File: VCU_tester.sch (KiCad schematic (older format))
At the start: 49 parts, among them J1 Conn_01x04_Male, J12 Conn_01x08_Male, J13 Conn_01x08_Male, J14 USB_C_Receptacle, J15 USB_B_Micro, J2 Screw_Terminal_01x02, J500 Conn_01x10_Female, J501 Conn_01x08_Female, J502 Conn_01x08_Female, J503 Conn_01x08_Female, J504 Conn_01x08_Female, J505 Conn_01x08_Female, J507 Conn_02x18_Odd_Even, J7 Conn_01x04_Male, P8 BeagleBone_Black_Header, P9 BeagleBone_Black_Header, U1 REF3020, U6 DS3231MZ, U7 DS3231MZ

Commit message: better routing, tcan footprint, mount holes + silkscreen
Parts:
- added H1, H2, H3, H4, H5, H6: MountingHole, MountingHole:MountingHole_3.2mm_M3_ISO7380_Pad, symbol Mechanical:MountingHole
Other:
- note added: "Removed (TO REASSIGN):\n J507-4 (adc) to GPIO_45\n J507-5 (adc) to GPIO_46\n J507-9 (uart) to GPIO_50\n J507-10 (nc) to GPIO_51"
- note added: "TODO:\n0) Assign new GPIOs on VCU\n1) ADD SILKSCREEN FOR WHAT TESTPOINTS ARE!!! (GPIO out of VCU??)"
- note removed: "Changes made (Andrew):\nPD25 (J500-3) fixed to VCURXD2A\nPressLin,PressLout moved to correct pins\nJ507-10 corrected to NC\nConnection to RTC Beagle fixed: SCL/SDA swapped\nRemoved:\n J507-4 (adc) to GPIO_45\n J507-5 (adc) to GPIO_46\n J507-9 (uart) to GPIO_50\n J507-10 (nc) to GPIO_51"
- note removed: "Changes made (Will):\nBoard initial layout done (NEED GPIOs)\nChanged power bus\n"
- note removed: "TODO:\n0) Assign new GPIOs on VCU\n1) ADD RES TO CP1/2 ON USBC\n2) ADD SILKSCREEN FOR WHAT TESTPOINTS ARE!!! (GPIO out of VCU??)"
- note removed: "\nReview gpio assignments\n"
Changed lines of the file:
@@
 Wire Wire Line
 	2800 7450 3700 7450
-Text Notes -2600 -2800 0    100  ~ 0
-Changes made (Andrew):\nPD25 (J500-3) fixed to VCURXD2A\nPressLin,PressLout moved to correct pins\nJ507-10 corrected to NC\nConnection to RTC Beagle fixed: SCL/SDA swapped\nRemoved:\n  J507-4 (adc) to GPIO_45\n  J507-5 (adc) to GPIO_46\n  J507-9 (uart) to GPIO_50\n  J507-10 (nc) to GPIO_51
+Text Notes -2600 -600 0    100  ~ 0
+Removed (TO REASSIGN):\n  J507-4 (adc) to GPIO_45\n  J507-5 (adc) to GPIO_46\n  J507-9 (uart) to GPIO_50\n  J507-10 (nc) to GPIO_51
 NoConn ~ 5300 7350
 NoConn ~ 5300 7450
@@
 NoConn ~ 5800 7550
 NoConn ~ 5800 7450
-Text Notes -2600 -950 0    100  ~ 0
-\nReview gpio assignments\n
 NoConn ~ 5300 8550
 Text Notes 5850 8550 0    50   ~ 0
@@
 	0    -1   -1   0
 $EndComp
-Text Notes 5450 -400 0    197  Italic 39
+Text Notes -4950 -2450 0    197  Italic 39
 wtf is up with VCU{TX,RX}D2 and VCU{TX,RX}D2A ???
 $Comp
@@
 $EndComp
 Text Notes -2600 -1750 0    79   ~ 16
-TODO:\n0) Assign new GPIOs on VCU\n1) ADD RES TO CP1/2 ON USBC\n2) ADD SILKSCREEN FOR WHAT TESTPOINTS ARE!!! (GPIO out of VCU??)
-Text Notes 2100 -1900 0    100  ~ 0
-Changes made (Will):\nBoard initial layout done (NEED GPIOs)\nChanged power bus\n
+TODO:\n0) Assign new GPIOs on VCU\n1) ADD SILKSCREEN FOR WHAT TESTPOINTS ARE!!! (GPIO out of VCU??)
 $Comp
 L Device:C C10
@@
 Connection ~ 8400 9950
 Connection ~ 9100 8200
+$Comp
+L Mechanical:MountingHole H5
+U 1 1 5F44CF3E
+P 4500 4550
+F 0 "H5" H 4600 4596 50  0000 L CNN
+F 1 "MountingHole" H 4600 4505 50  0000 L CNN
+F 2 "MountingHole:MountingHole_3.2mm_M3_ISO7380_Pad" H 4500 4550 50  0001 C CNN
+F 3 "~" H 4500 4550 50  0001 C CNN
+	1    4500 4550
+	1    0    0    -1
+$EndComp
+$Comp
+L Mechanical:MountingHole H6
+U 1 1 5F453185
+P 4500 4750
+F 0 "H6" H 4600 4796 50  0000 L CNN
+F 1 "MountingHole" H 4600 4705 50  0000 L CNN
+F 2 "MountingHole:MountingHole_3.2mm_M3_ISO7380_Pad" H 4500 4750 50  0001 C CNN
+F 3 "~" H 4500 4750 50  0001 C CNN
+	1    4500 4750
+	1    0    0    -1
+$EndComp
+$Comp
+L Mechanical:MountingHole H1
+U 1 1 5F4A1F4C
+P 3800 4550
+F 0 "H1" H 3900 4596 50  0000 L CNN
+F 1 "MountingHole" H 3900 4505 50  0000 L CNN
+F 2 "MountingHole:MountingHole_3.2mm_M3_ISO7380_Pad" H 3800 4550 50  0001 C CNN
+F 3 "~" H 3800 4550 50  0001 C CNN
+	1    3800 4550
+	1    0    0    -1
+$EndComp
+$Comp
+L Mechanical:MountingHole H2
+U 1 1 5F4BC44A
+P 3800 4750
+F 0 "H2" H 3900 4796 50  0000 L CNN
+F 1 "MountingHole" H 3900 4705 50  0000 L CNN
+F 2 "MountingHole:MountingHole_3.2mm_M3_ISO7380_Pad" H 3800 4750 50  0001 C CNN
+F 3 "~" H 3800 4750 50  0001 C CNN
+	1    3800 4750
+	1    0    0    -1
+$EndComp
+$Comp
+L Mechanical:MountingHole H3
+U 1 1 5F4D68CE
+P 3800 4950
+F 0 "H3" H 3900 4996 50  0000 L CNN
+F 1 "MountingHole" H 3900 4905 50  0000 L CNN
+F 2 "MountingHole:MountingHole_3.2mm_M3_ISO7380_Pad" H 3800 4950 50  0001 C CNN
+F 3 "~" H 3800 4950 50  0001 C CNN
+	1    3800 4950
+	1    0    0    -1
+$EndComp
+$Comp
+L Mechanical:MountingHole H4
+U 1 1 5F4F0D27
+P 3800 5150
+F 0 "H4" H 3900 5196 50  0000 L CNN
+F 1 "MountingHole" H 3900 5105 50  0000 L CNN
+F 2 "MountingHole:MountingHole_3.2mm_M3_ISO7380_Pad" H 3800 5150 50  0001 C CNN
+F 3 "~" H 3800 5150 50  0001 C CNN
+	1    3800 5150
+	1    0    0    -1
+$EndComp
 $EndSCHEMATC

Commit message: reassigned brake, emsdc, audio vcurst, better testpoint
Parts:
- removed TP2, TP4, TP43, TP45, TP46: TestPoint, Connector_PinHeader_2.54mm:PinHeader_1x01_P2.54mm_Vertical, symbol Connector:TestPoint
- added J16: Conn_01x05_Male, Connector_PinHeader_2.54mm:PinHeader_1x05_P2.54mm_Vertical, symbol Connector:Conn_01x05_Male
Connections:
- net GPIO_4 is gone; now on net GPIO_23: J500.2 (Pin_2)
- net GPIO_7 is gone; now on net GPIO_27: J503.7 (Pin_7)
- net GNDD: now also J16.5 (Pin_5)
- net GPIO_112: now also J16.4 (Pin_4)
- net GPIO_23: now also J16.1 (Pin_1)
- net GPIO_27: now also J16.2 (Pin_2)
- net GPIO_5 renamed GPIO_28
- net GPIO_28: now also J16.3 (Pin_3)
- no-connect marks 123 -> 120
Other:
- note added: "changed:\ngpio 23, 26, 27 routed to brake, ass and audio"
- note removed: "GPIO_4"
- note removed: "GPIO_5"
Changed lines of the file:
@@
 Wire Wire Line
 	14200 6100 13700 6100
-Text Label 14200 6500 2    50   ~ 0
-GPIO_7
-Text Label 14200 6400 2    50   ~ 0
-GPIO_5
-Text Label 14200 6200 2    50   ~ 0
-GPIO_4
-$Comp
-L Connector:TestPoint TP?
-U 1 1 5F7539BC
-P 13700 6200
-AR Path="/5ED986AC/5F7539BC" Ref="TP?"  Part="1"
-AR Path="/5F7539BC" Ref="TP43"  Part="1"
-F 0 "TP43" V 13750 6800 50  0000 L CNN
-F 1 "TestPoint" V 13750 6400 50  0000 L CNN
-F 2 "Connector_PinHeader_2.54mm:PinHeader_1x01_P2.54mm_Vertical" H 13900 6200 50  0001 C CNN
-F 3 "~" H 13900 6200 50  0001 C CNN
-	1    13700 6200
-	0    -1   -1   0
-$EndComp
-Wire Wire Line
-	13700 6200 14200 6200
-$Comp
-L Connector:TestPoint TP?
-U 1 1 5F7539C4
-P 13700 6500
-AR Path="/5ED986AC/5F7539C4" Ref="TP?"  Part="1"
-AR Path="/5F7539C4" Ref="TP46"  Part="1"
-F 0 "TP46" V 13750 7100 50  0000 L CNN
-F 1 "TestPoint" V 13750 6700 50  0000 L CNN
-F 2 "Connector_PinHeader_2.54mm:PinHeader_1x01_P2.54mm_Vertical" H 13900 6500 50  0001 C CNN
-F 3 "~" H 13900 6500 50  0001 C CNN
-	1    13700 6500
-	0    -1   -1   0
-$EndComp
-$Comp
-L Connector:TestPoint TP?
-U 1 1 5F7539CA
-P 13700 6400
-AR Path="/5ED986AC/5F7539CA" Ref="TP?"  Part="1"
-AR Path="/5F7539CA" Ref="TP45"  Part="1"
-F 0 "TP45" V 13750 7000 50  0000 L CNN
-F 1 "TestPoint" V 13750 6600 50  0000 L CNN
-F 2 "Connector_PinHeader_2.54mm:PinHeader_1x01_P2.54mm_Vertical" H 13900 6400 50  0001 C CNN
-F 3 "~" H 13900 6400 50  0001 C CNN
-	1    13700 6400
-	0    -1   -1   0
-$EndComp
-Wire Wire Line
-	14200 6500 13700 6500
-Wire Wire Line
-	13700 6400 14200 6400
+Text Label 15500 5600 2    50   ~ 0
+GPIO_28
+Text Label 15500 5500 2    50   ~ 0
+GPIO_27
+Text Label 15500 5400 2    50   ~ 0
+GPIO_23
+Wire Wire Line
+	15000 5400 15500 5400
+Wire Wire Line
+	15500 5600 15000 5600
+Wire Wire Line
+	15000 5500 15500 5500
 Text Label 14200 6700 2    47   ~ 0
 UART1_TXD
@@
 	13700 6600 14200 6600
 NoConn ~ 5400 1650
-NoConn ~ 4100 1950
-NoConn ~ 5400 1950
-NoConn ~ 4100 2150
 NoConn ~ 3100 2650
 NoConn ~ 1800 2850
@@
 $Comp
 L Connector:TestPoint TP?
-U 1 1 5EA02E7E
-P 1650 7050
-AR Path="/5ED986AC/5EA02E7E" Ref="TP?"  Part="1"
-AR Path="/5EA02E7E" Ref="TP2"  Part="1"
-F 0 "TP2" H 1500 7150 50  0000 L CNN
-F 1 "TestPoint" H 1700 7150 50  0000 L CNN
-F 2 "Connector_PinHeader_2.54mm:PinHeader_1x01_P2.54mm_Vertical" H 1850 7050 50  0001 C CNN
-F 3 "~" H 1850 7050 50  0001 C CNN
-	1    1650 7050
-	-1   0    0    1
-$EndComp
-$Comp
-L Connector:TestPoint TP?
 U 1 1 5EA253A5
 P 1600 6950
@@
 	1400 6950 1600 6950
 Connection ~ 1600 6950
-Wire Wire Line
-	1400 7050 1650 7050
-Wire Wire Line
-	1650 7050 1900 7050
-Connection ~ 1650 7050
 NoConn ~ 1900 6850
 Text Label 2800 8450 2    47   ~ 0
@@
 	1    5300 9100
 	-1   0    0    1
-$EndComp
-$Comp
-L Connector:TestPoint TP?
-U 1 1 5F9D6AC5
-P 6100 6900
-AR Path="/5ED986AC/5F9D6AC5" Ref="TP?"  Part="1"
-AR Path="/5F9D6AC5" Ref="TP4"  Part="1"
-F 0 "TP4" H 6158 7018 50  0000 L CNN
-F 1 "TestPoint" H 6158 6927 50  0000 L CNN
-F 2 "Connector_PinHeader_2.54mm:PinHeader_1x01_P2.54mm_Vertical" H 6300 6900 50  0001 C CNN
-F 3 "~" H 6300 6900 50  0001 C CNN
-	1    6100 6900
-	1    0    0    -1
 $EndComp
 NoConn ~ 1900 8650
@@
 PressRin
 Text Label 2800 7850 2    50   ~ 0
-GPIO_7
+GPIO_27
 Text Label 2800 7750 2    50   ~ 0
-GPIO_5
+GPIO_28
 Text Label 2800 7450 2    50   ~ 0
-GPIO_4
+GPIO_23
 Text Notes 3900 7850 0    50   ~ 0
 ASSTrip
@@
 Text Label 1800 2150 0    50   ~ 0
 I2C1_SCL
-Text Notes 1750 2150 2    50   ~ 0
-GPIO_5
-Text Notes 3150 2150 0    50   ~ 0
-GPIO_4
 Text Label 7800 3900 2    50   ~ 0
 I2C1_SDA
@@
 	1    0    0    -1
 $EndComp
+Text Notes -2700 -150 0    50   ~ 0
+changed:\ngpio 23, 26, 27 routed to brake, ass and audio
+Wire Wire Line
+	1400 7050 1900 7050
+Text Label 15500 5700 2    50   ~ 0
+VCURESET
+$Comp
+L Connector:Conn_01x05_Male J16
+U 1 1 5E67BBA1
+P 14800 5600
+F 0 "J16" H 14908 5981 50  0000 C CNN
+F 1 "Conn_01x05_Male" H 14908 5890 50  0000 C CNN
+F 2 "Connector_PinHeader_2.54mm:PinHeader_1x05_P2.54mm_Vertical" H 14800 5600 50  0001 C CNN
+F 3 "~" H 14800 5600 50  0001 C CNN
+	1    14800 5600
+	1    0    0    -1
+$EndComp
+Wire Wire Line
+	15500 5700 15000 5700
+Wire Wire Line
+	15000 5800 15400 5800
+Wire Wire Line
+	15400 5800 15400 5900
+$Comp
+L power:GNDD #PWR024
+U 1 1 5E6B0A81
+P 15400 5900
+F 0 "#PWR024" H 15400 5650 50  0001 C CNN
+F 1 "GNDD" H 15404 5745 50  0000 C CNN
+F 2 "" H 15400 5900 50  0001 C CNN
+F 3 "" H 15400 5900 50  0001 C CNN
+	1    15400 5900
+	1    0    0    -1
+$EndComp

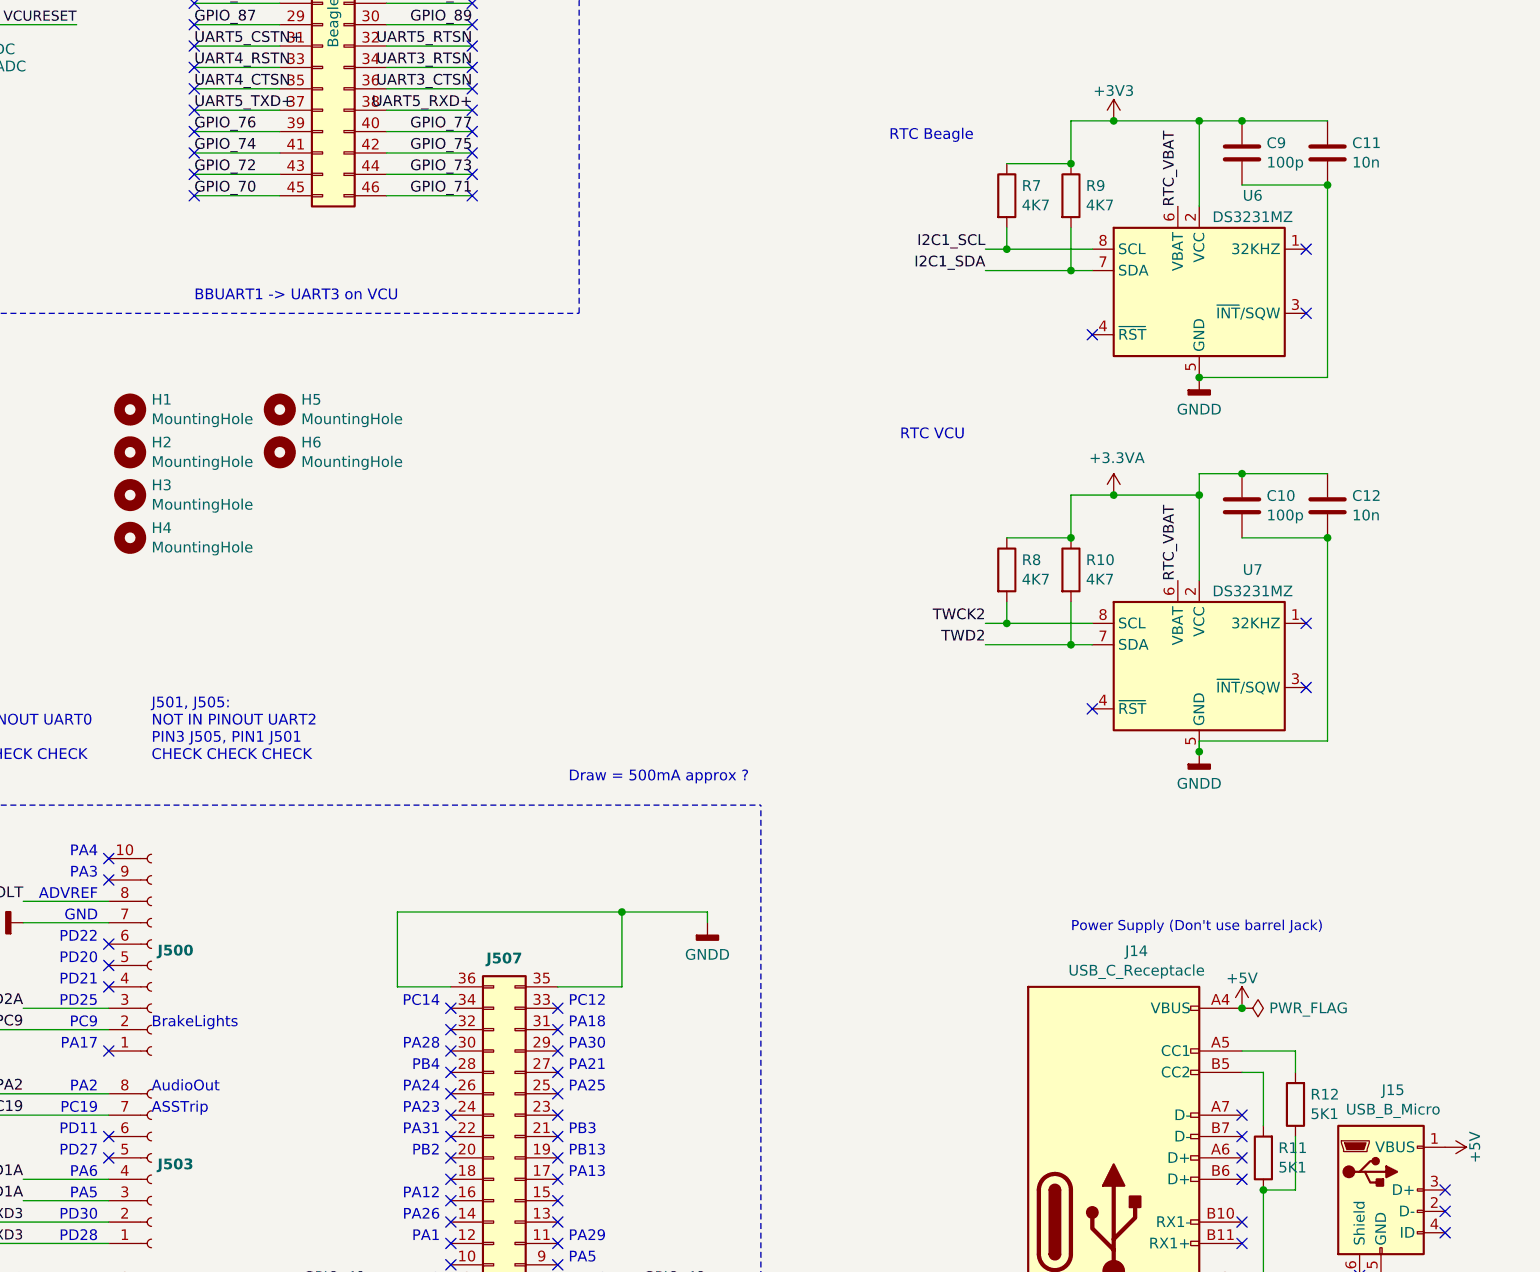
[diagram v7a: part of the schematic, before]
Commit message: add decouple caps, add gpios
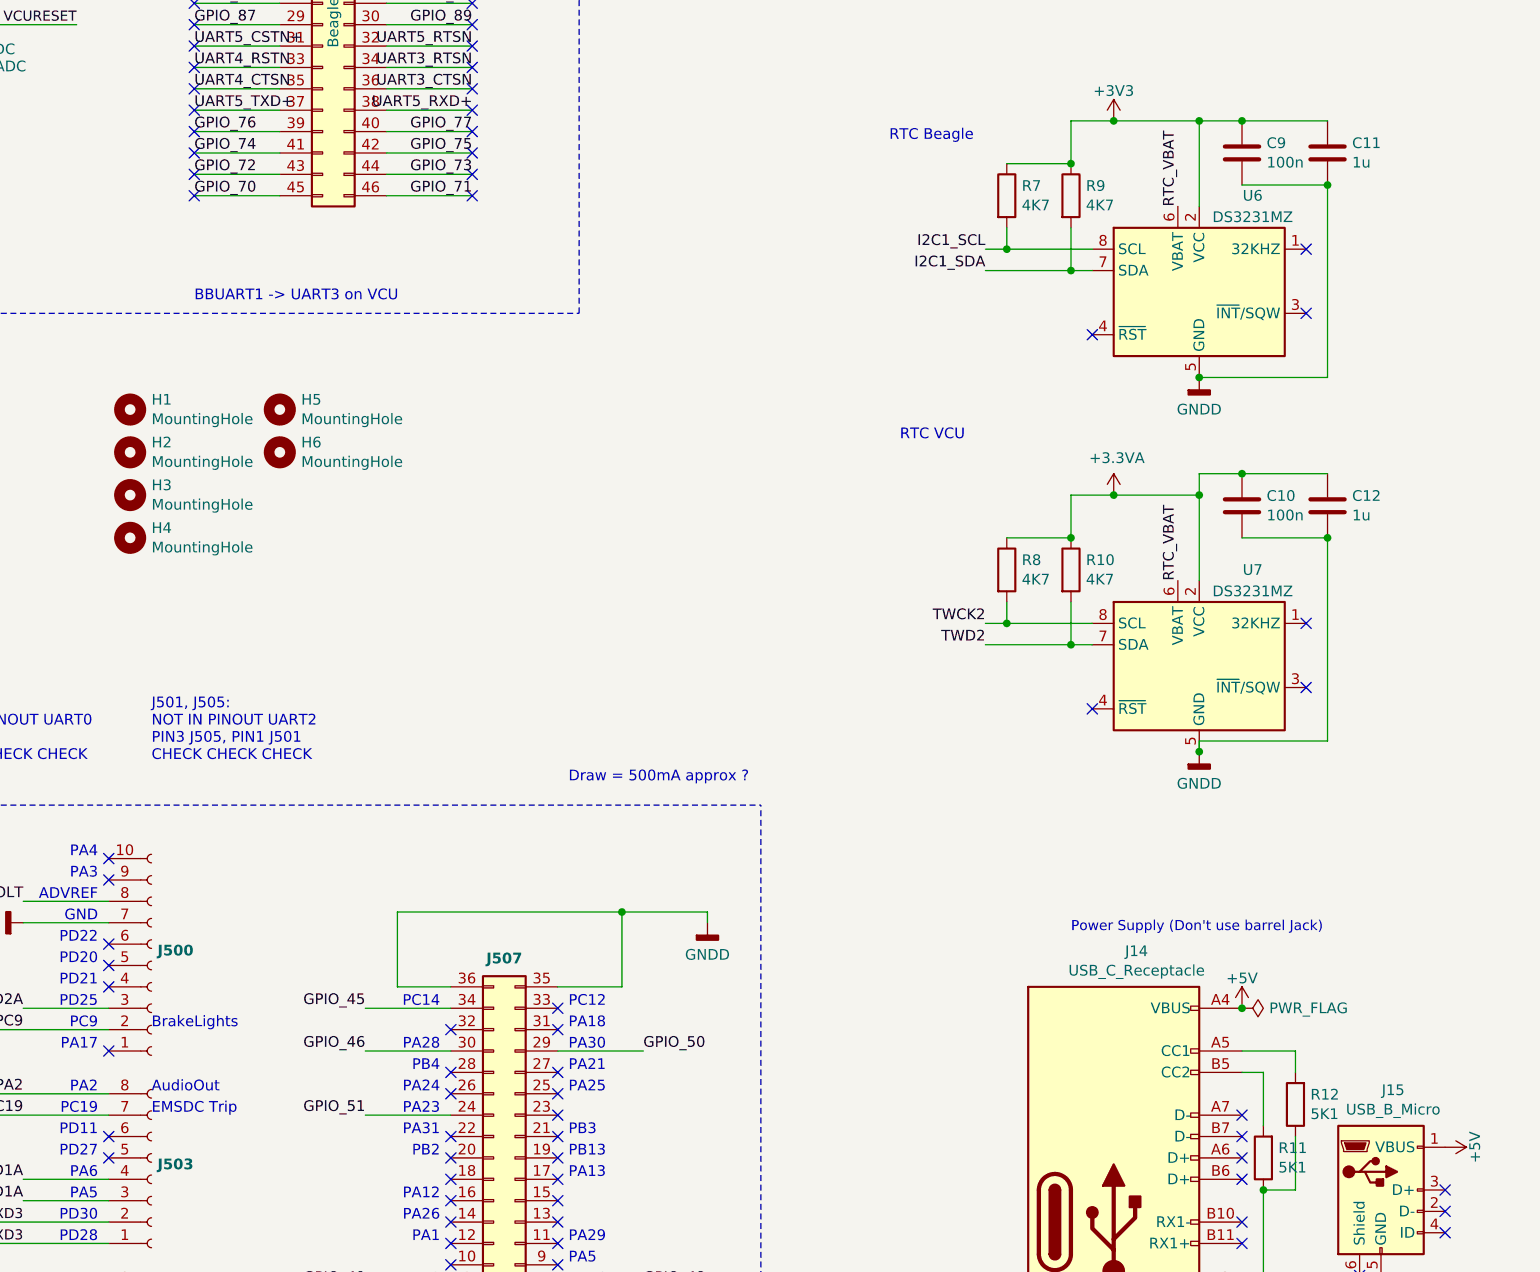
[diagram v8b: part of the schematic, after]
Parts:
- C10, C9: value 100p -> 100n
- C11, C12: value 10n -> 1u
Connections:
- net GPIO_45: now also J507.34 (Pin_34)
- net GPIO_46: now also J507.30 (Pin_30)
- net GPIO_50: now also J507.29 (Pin_29)
- net GPIO_51: now also J507.24 (Pin_24)
- no-connect marks 120 -> 116
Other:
- note added: "EMSDC Trip"
- note removed: "ASSTrip"
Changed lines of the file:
@@
 NoConn ~ 5300 8450
 NoConn ~ 5300 7750
-NoConn ~ 5300 7850
 NoConn ~ 5300 7950
 NoConn ~ 5300 8050
@@
 GPIO_23
 Text Notes 3900 7850 0    50   ~ 0
-ASSTrip
+EMSDC Trip
 $Comp
 L Connector:Conn_01x10_Female J500
@@
 Text Notes -2600 -600 0    100  ~ 0
 Removed (TO REASSIGN):\n  J507-4 (adc) to GPIO_45\n  J507-5 (adc) to GPIO_46\n  J507-9 (uart) to GPIO_50\n  J507-10 (nc) to GPIO_51
-NoConn ~ 5300 7350
 NoConn ~ 5300 7450
-NoConn ~ 5300 7550
 NoConn ~ 5300 7650
-NoConn ~ 5800 7550
 NoConn ~ 5800 7450
 NoConn ~ 5300 8550
@@
 P 9000 5000
 F 0 "C10" H 9115 5046 50  0000 L CNN
-F 1 "100p" H 9115 4955 50  0000 L CNN
+F 1 "100n" H 9115 4955 50  0000 L CNN
 F 2 "Capacitor_SMD:C_0805_2012Metric_Pad1.15x1.40mm_HandSolder" H 9038 4850 50  0001 C CNN
 F 3 "~" H 9000 5000 50  0001 C CNN
@@
 P 9400 5000
 F 0 "C12" H 9515 5046 50  0000 L CNN
-F 1 "10n" H 9515 4955 50  0000 L CNN
+F 1 "1u" H 9515 4955 50  0000 L CNN
 F 2 "Capacitor_SMD:C_0805_2012Metric_Pad1.15x1.40mm_HandSolder" H 9438 4850 50  0001 C CNN
 F 3 "~" H 9400 5000 50  0001 C CNN
@@
 P 9000 3350
 F 0 "C9" H 9115 3396 50  0000 L CNN
-F 1 "100p" H 9115 3305 50  0000 L CNN
+F 1 "100n" H 9115 3305 50  0000 L CNN
 F 2 "Capacitor_SMD:C_0805_2012Metric_Pad1.15x1.40mm_HandSolder" H 9038 3200 50  0001 C CNN
 F 3 "~" H 9000 3350 50  0001 C CNN
@@
 P 9400 3350
 F 0 "C11" H 9515 3396 50  0000 L CNN
-F 1 "10n" H 9515 3305 50  0000 L CNN
+F 1 "1u" H 9515 3305 50  0000 L CNN
 F 2 "Capacitor_SMD:C_0805_2012Metric_Pad1.15x1.40mm_HandSolder" H 9438 3200 50  0001 C CNN
 F 3 "~" H 9400 3350 50  0001 C CNN
@@
 	1    0    0    -1
 $EndComp
+Wire Wire Line
+	5300 7350 4900 7350
+Wire Wire Line
+	5800 7550 6200 7550
+Wire Wire Line
+	5300 7550 4900 7550
+Wire Wire Line
+	5300 7850 4900 7850
+Text Label 6200 7550 0    50   ~ 0
+GPIO_50
+Text Label 4900 7850 2    50   ~ 0
+GPIO_51
+Text Label 4900 7350 2    50   ~ 0
+GPIO_45
+Text Label 4900 7550 2    50   ~ 0
+GPIO_46
 $EndSCHEMATC
